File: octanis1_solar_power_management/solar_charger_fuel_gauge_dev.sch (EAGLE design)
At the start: 92 parts, among them IC401 TUSB2046BIRHBIRHB, Q2 32.768kHz, Q4 CSTCR4M00G15L99, Q401 CSTCR6M00G15L99, U1 BQ24210, U2 BQ27510_DRZ_12, U402 TPS62237DRY, U404 TPD2E001DRLR, U6 MSP430F5529IPNR

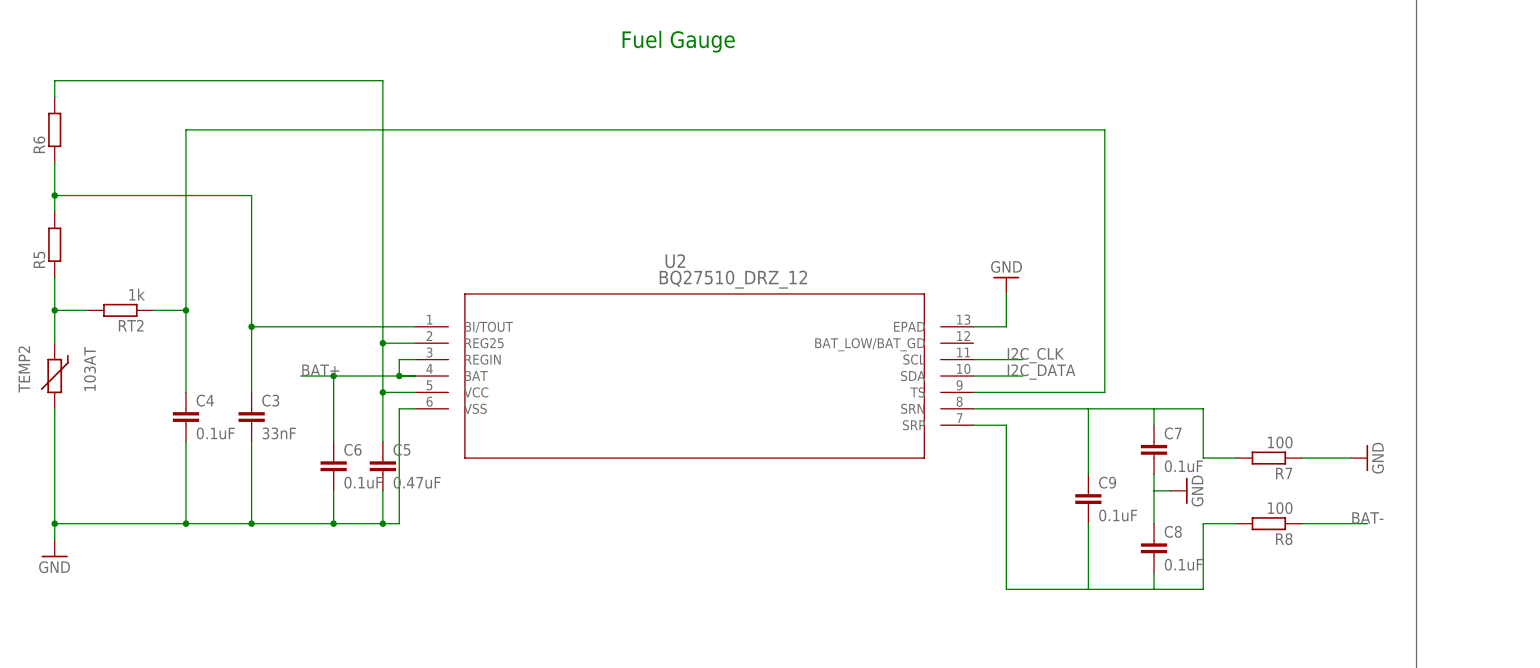
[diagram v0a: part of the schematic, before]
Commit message: Renamed and placed Parts for fuel gauge part of circuit
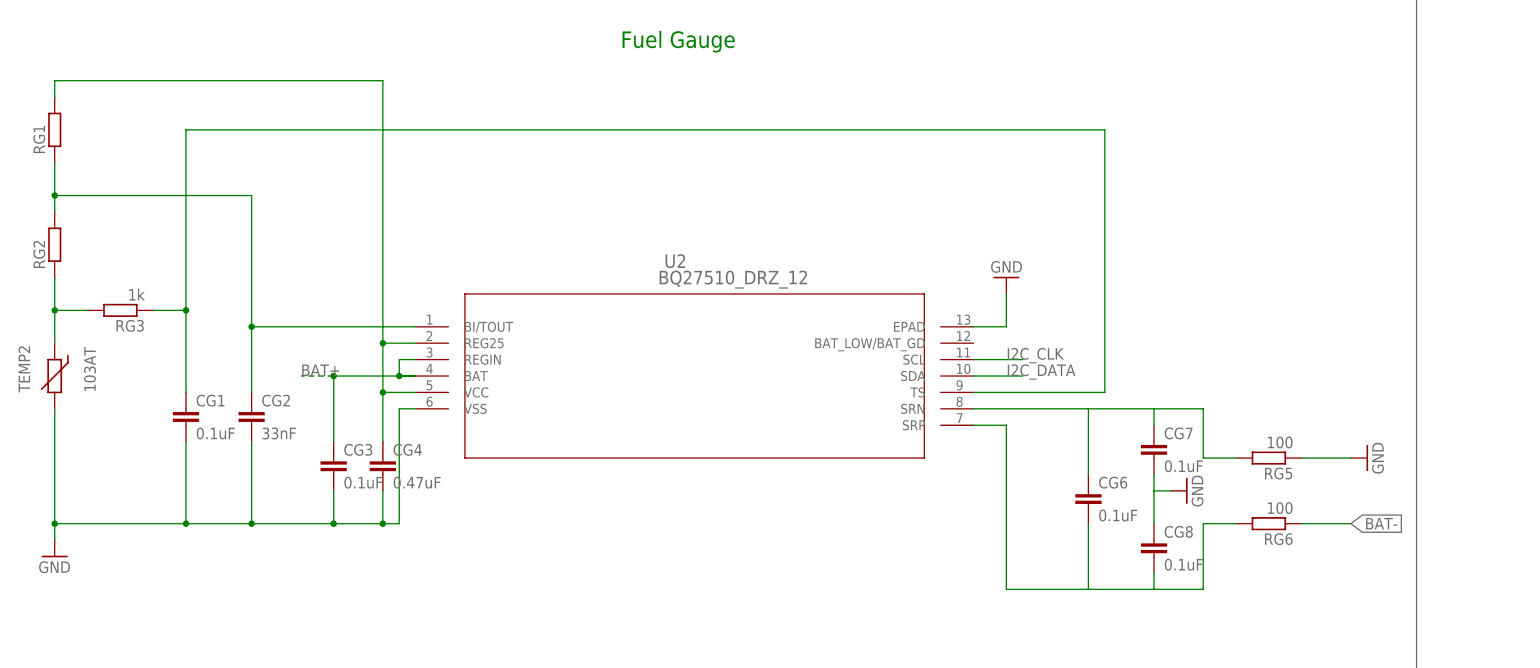
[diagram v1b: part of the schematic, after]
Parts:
- renumbered C3 to CG2, C4 to CG1, C5 to CG4, C6 to CG3, C7 to CG7, C8 to CG8, C9 to CG6, R5 to RG2, R6 to RG1, R7 to RG5, R8 to RG6, RT2 to RG3

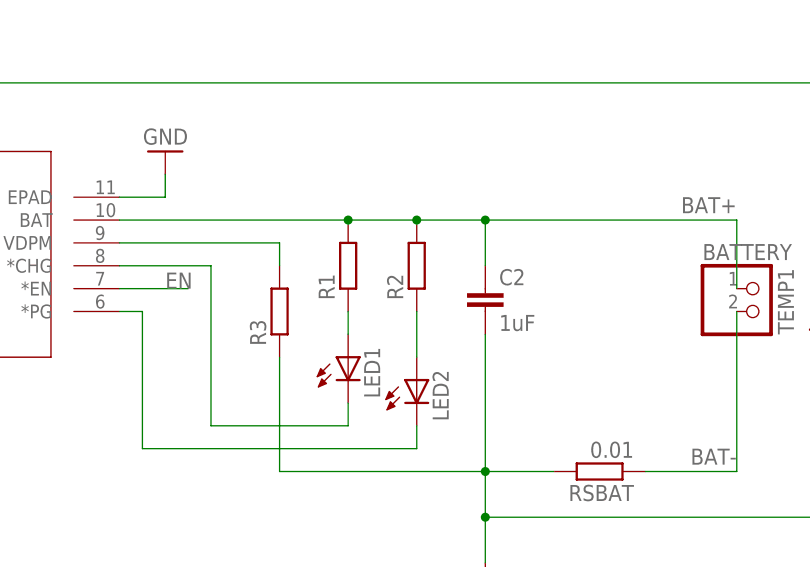
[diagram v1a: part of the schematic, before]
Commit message: Rearranged some components and routes and increased thickness of power lines
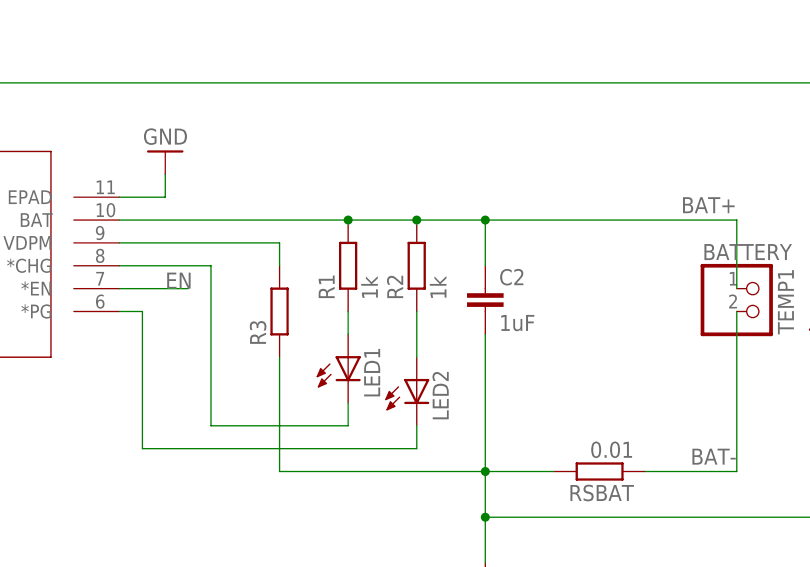
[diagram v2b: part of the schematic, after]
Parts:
- R1, R2: value (none) -> 1k
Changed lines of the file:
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@@
 </class>
 <class number="1" name="Ground" width="0.2032" drill="0.3048">
-<clearance class="0" value="0.1524"/>
 <clearance class="1" value="0.1524"/>
 </class>
 <class number="2" name="Power" width="0.2032" drill="0.3048">
+<clearance class="2" value="0.1524"/>
+</class>
+<class number="3" name="hPower" width="0.4064" drill="0.6096">
+<clearance class="3" value="0.1524"/>
+</class>
+<class number="4" name="hGround" width="0.4064" drill="0.6096">
 <clearance class="0" value="0.1524"/>
-<clearance class="1" value="0.1524"/>
-<clearance class="2" value="0.1524"/>
+<clearance class="4" value="0.1524"/>
 </class>
 </classes>
@@
 <part name="LED1" library="led" deviceset="LED" device="CHIP-LED0603"/>
 <part name="LED2" library="led" deviceset="LED" device="CHIP-LED0603"/>
-<part name="R1" library="resistor" deviceset="R-EU_" device="R1206"/>
-<part name="R2" library="resistor" deviceset="R-EU_" device="R1206"/>
+<part name="R1" library="resistor" deviceset="R-EU_" device="R1206" value="1k"/>
+<part name="R2" library="resistor" deviceset="R-EU_" device="R1206" value="1k"/>
 <part name="TEMP1" library="varistor" deviceset="THERMISTOR" device="-2,5" value="103AT"/>
 <part name="RT1" library="resistor" deviceset="R-EU_" device="R1206"/>
@@
 </segment>
 </net>
-<net name="BAT+" class="1">
+<net name="BAT+" class="3">
 <segment>
 <pinref part="U1" gate="A" pin="BAT"/>
@@
 </segment>
 </net>
-<net name="N$13" class="0">
+<net name="N$13" class="3">
 <segment>
 <pinref part="U1" gate="A" pin="VBUS"/>

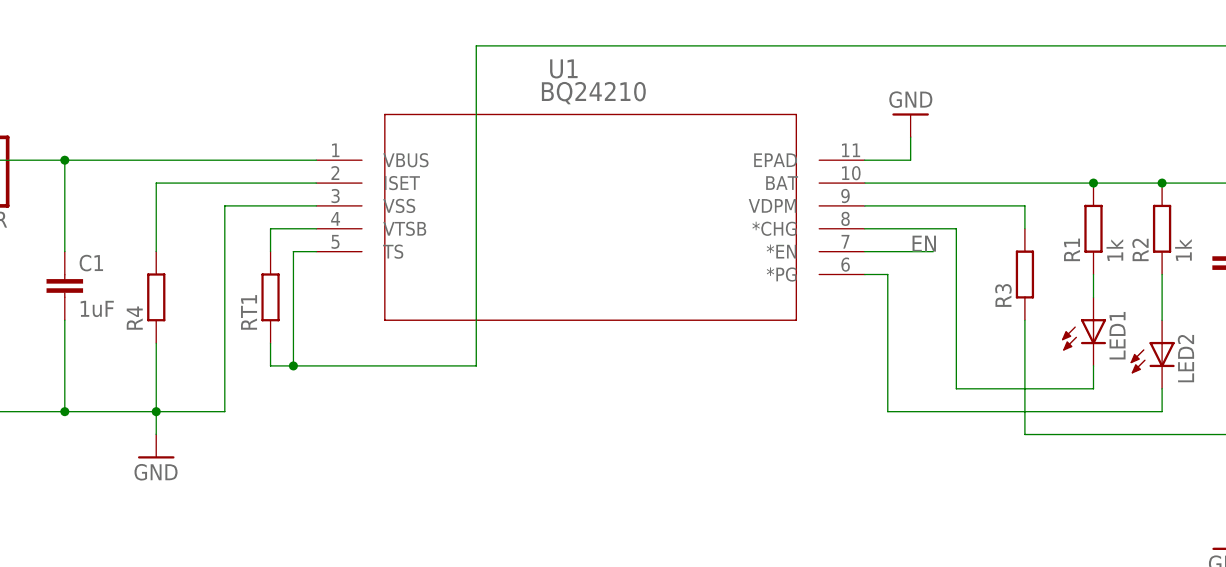
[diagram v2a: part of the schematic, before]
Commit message: Calculated R-values for Battery chargin circuit
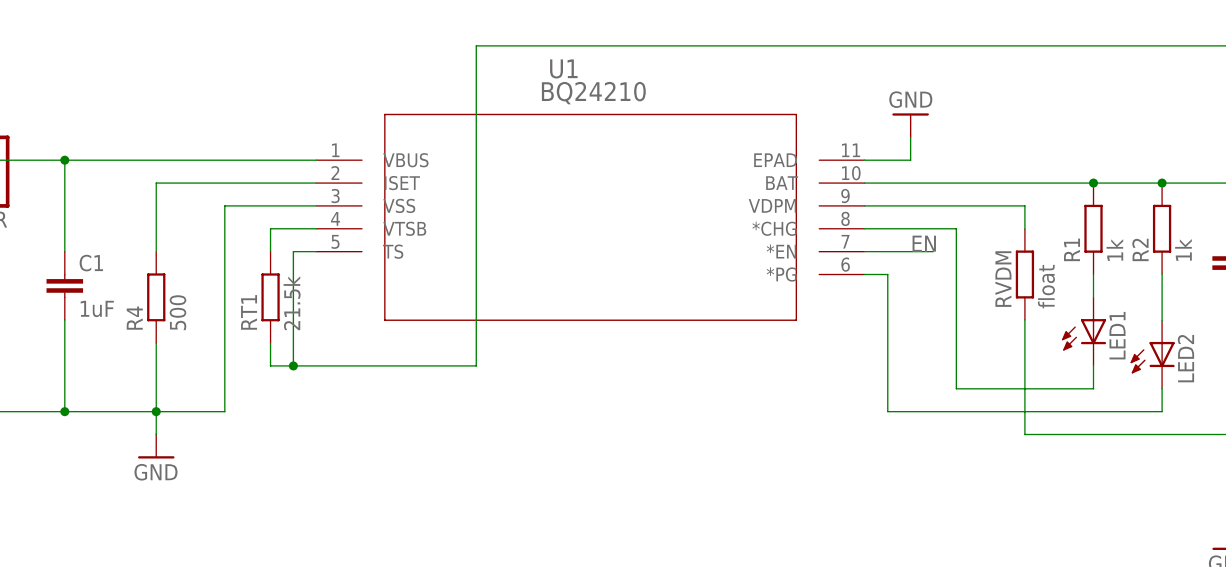
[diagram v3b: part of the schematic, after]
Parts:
- R4: value (none) -> 500
- RT1: value (none) -> 21.5k
- RVDM: value (none) -> float
- renumbered R3 to RVDM
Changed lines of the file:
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@@
 <part name="R2" library="resistor" deviceset="R-EU_" device="R1206" value="1k"/>
 <part name="TEMP1" library="varistor" deviceset="THERMISTOR" device="-2,5" value="103AT"/>
-<part name="RT1" library="resistor" deviceset="R-EU_" device="R1206"/>
+<part name="RT1" library="resistor" deviceset="R-EU_" device="R1206" value="21.5k"/>
 <part name="BATTERY" library="pinhead" deviceset="PINHD-1X2" device=""/>
-<part name="R3" library="resistor" deviceset="R-EU_" device="R1206"/>
-<part name="R4" library="resistor" deviceset="R-EU_" device="R1206"/>
+<part name="RVDM" library="resistor" deviceset="R-EU_" device="R1206" value="float"/>
+<part name="R4" library="resistor" deviceset="R-EU_" device="R1206" value="500"/>
 <part name="SOLAR" library="pinhead" deviceset="PINHD-1X2" device=""/>
 <part name="U2" library="bq27510_drz_12" deviceset="BQ27510_DRZ_12" device=""/>
@@
 <instance part="RT1" gate="G$1" x="20.32" y="68.58" rot="R90"/>
 <instance part="BATTERY" gate="G$1" x="157.48" y="71.12"/>
-<instance part="R3" gate="G$1" x="104.14" y="71.12" rot="R90"/>
+<instance part="RVDM" gate="G$1" x="104.14" y="71.12" rot="R90"/>
 <instance part="R4" gate="G$1" x="7.62" y="68.58" rot="R90"/>
 <instance part="SOLAR" gate="G$1" x="-15.24" y="83.82" rot="R180"/>
@@
 <wire x1="127" y1="68.58" x2="127" y2="53.34" width="0.1524" layer="91"/>
 <pinref part="GND3" gate="1" pin="GND"/>
-<pinref part="R3" gate="G$1" pin="1"/>
+<pinref part="RVDM" gate="G$1" pin="1"/>
 <wire x1="104.14" y1="66.04" x2="104.14" y2="53.34" width="0.1524" layer="91"/>
 <wire x1="104.14" y1="53.34" x2="127" y2="53.34" width="0.1524" layer="91"/>
@@
 <segment>
 <pinref part="U1" gate="A" pin="VDPM"/>
-<pinref part="R3" gate="G$1" pin="2"/>
+<pinref part="RVDM" gate="G$1" pin="2"/>
 <wire x1="86.36" y1="78.74" x2="104.14" y2="78.74" width="0.1524" layer="91"/>
 <wire x1="104.14" y1="78.74" x2="104.14" y2="76.2" width="0.1524" layer="91"/>
